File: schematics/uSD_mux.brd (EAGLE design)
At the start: 43.5 x 43.2 mm, 15 parts

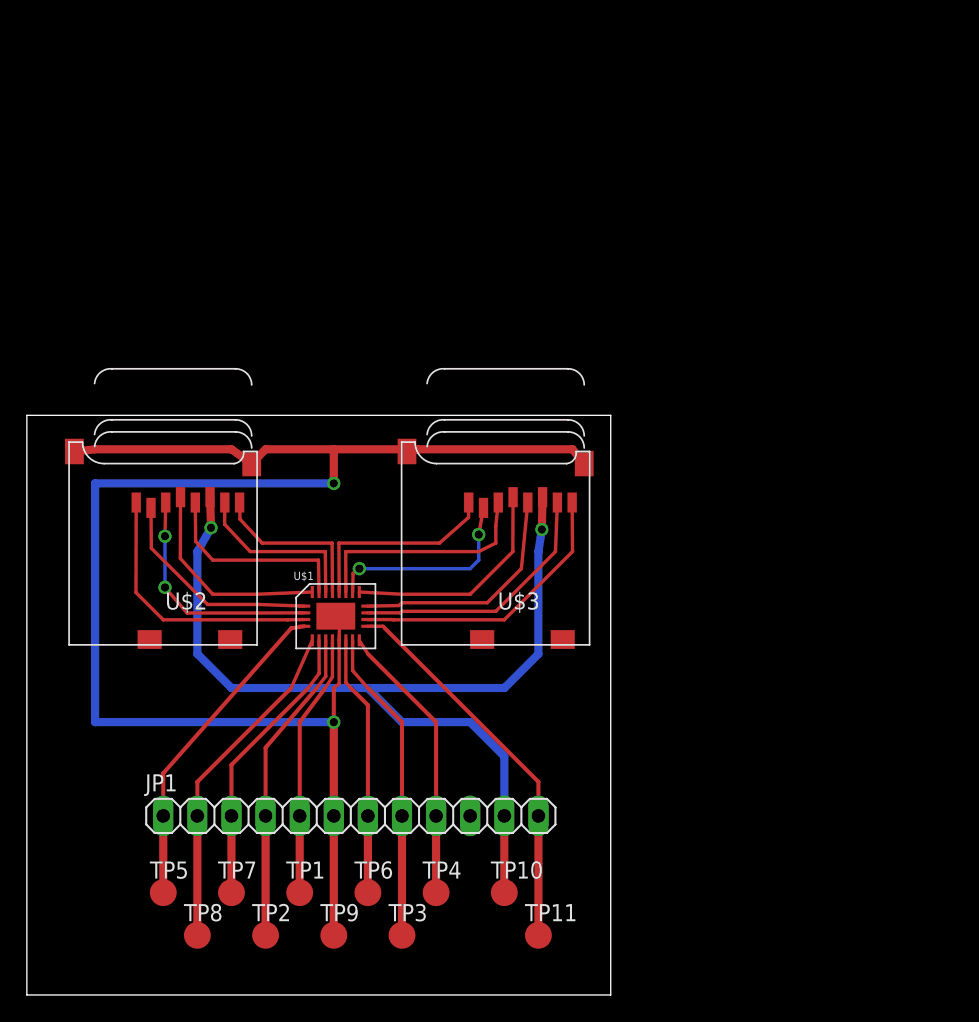
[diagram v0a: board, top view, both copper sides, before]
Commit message: Updated uSD mux board
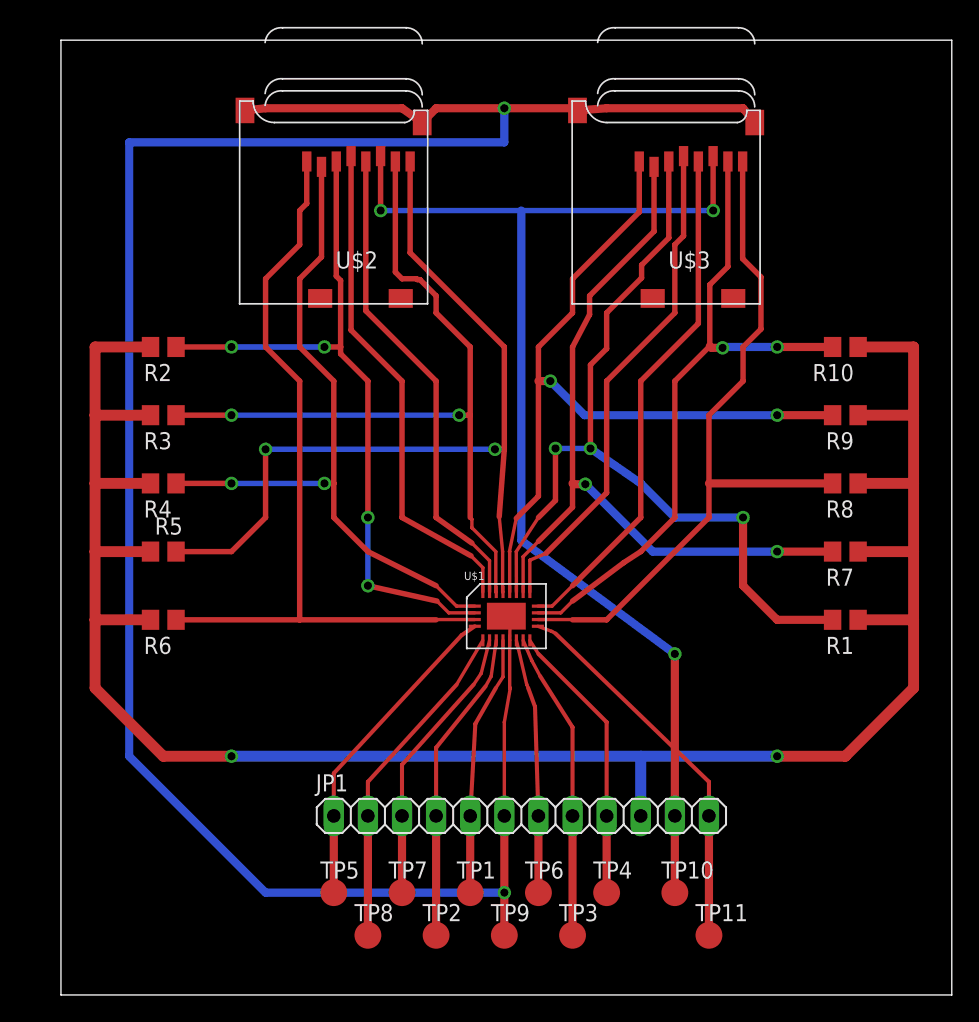
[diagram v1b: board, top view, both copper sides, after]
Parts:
- added R1, R10, R2, R3, R4, R5, R6, R7, R8, R9: 97k, rcl:R0805
- moved U$2 28.4 mm to (29.8, 51.4)
- moved U$3 28.4 mm to (54.6, 51.4)
- moved TP1 12.7 mm to (33.0, 7.62)
- moved TP6 12.7 mm to (38.1, 7.62)
- moved TP9 12.7 mm to (35.6, 4.45)
- moved U$1 12.7 mm to (35.6, 29.2)
- moved TP7 12.7 mm to (27.9, 7.62)
- moved JP1 12.7 mm to (36.8, 13.3)
- moved TP2 12.7 mm to (30.5, 4.45)
- moved TP3 12.7 mm to (40.6, 4.45)
- moved TP4 12.7 mm to (43.2, 7.62)
- moved TP5 12.7 mm to (22.9, 7.62)
- moved TP8 12.7 mm to (25.4, 4.45)
- moved TP10 12.7 mm to (48.3, 7.62)
- moved TP11 12.7 mm to (50.8, 4.45)
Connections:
- new net N$1: JP1.10, R1.1, R10.1, R2.2, R3.2, R4.2, R5.1, R6.2, R7.1, R8.1, R9.1
- net N$10: now also R8.2
- net N$11: now also R9.2
- net N$12: now also R1.2
- net N$2: now also R4.1
- net N$3: now also R3.1
- net N$4: now also R5.2
- net N$5: now also R6.1
- net N$6: now also R2.1
- net N$8: now also R7.2
- net N$9: now also R10.2
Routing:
- net N$1: track 0.00 -> 161.7 mm, vias 0 -> 2
- net N$4: track 12.5 -> 65.6 mm, vias 0 -> 2
- net GND: track 119.2 -> 171.5 mm
- net N$12: track 17.4 -> 64.1 mm, vias 0 -> 3
- net N$3: track 13.0 -> 57.9 mm, vias 0 -> 2
- net N$11: track 15.1 -> 58.9 mm, vias 0 -> 2
- net N$8: track 15.0 -> 57.0 mm
- net N$5: track 20.1 -> 58.7 mm
- net N$2: track 16.1 -> 52.4 mm, vias 0 -> 2
- net N$6: track 17.6 -> 53.3 mm, vias 2 -> 4
- net N$10: track 21.0 -> 53.8 mm
- net N$9: track 19.6 -> 50.2 mm, vias 0 -> 2
- net VDDC1: track 15.6 -> 37.4 mm
- net N$13: track 17.5 -> 38.7 mm
- net N$7: track 15.0 -> 36.1 mm
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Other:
- board size 43.5 x 43.2 mm -> 66.3 x 71.1 mm

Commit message: Updated uSD mux board layout
Forgot to check oshpark DRU before committing first time.  Made
revisions necessary to board layout to meet oshparks design rules.
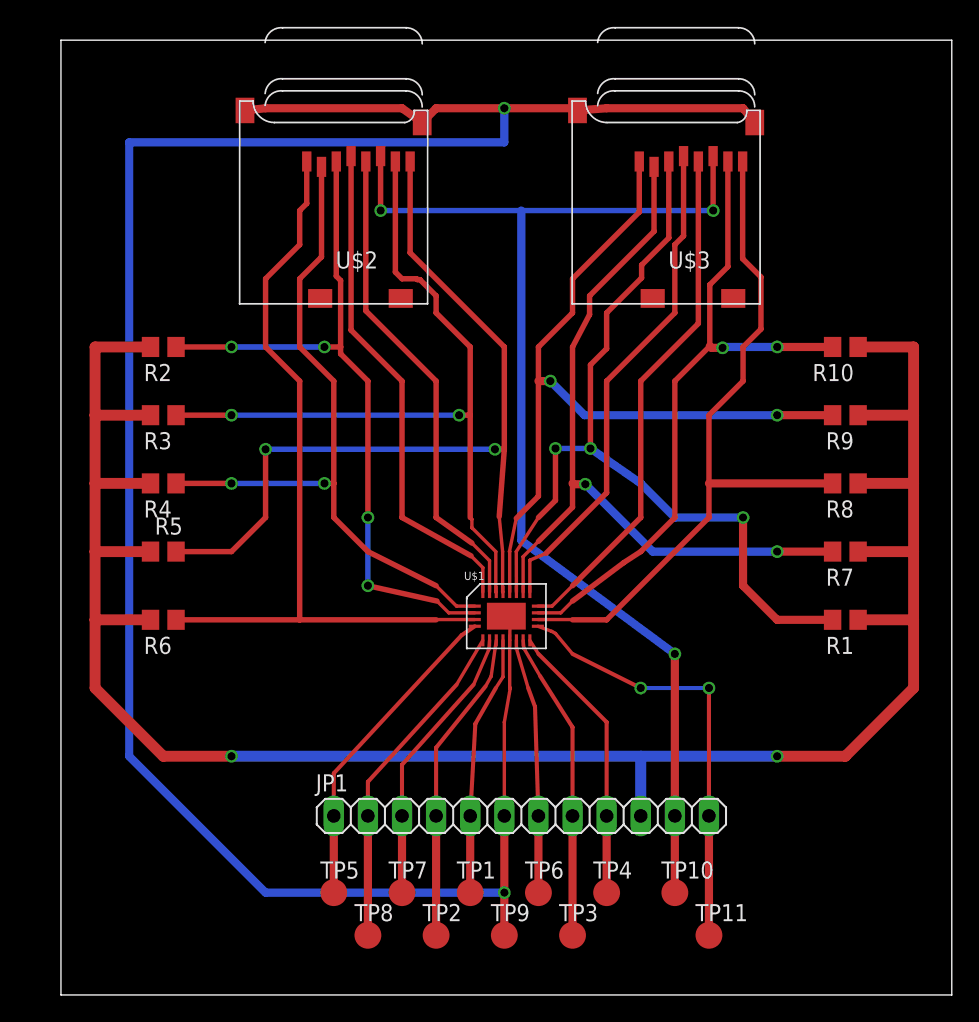
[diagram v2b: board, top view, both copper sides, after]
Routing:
- net S: track 28.7 -> 32.6 mm, vias 0 -> 2
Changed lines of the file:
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@@
 </class>
 </classes>
-<designrules name="epl-lpkf *">
-<description language="en">&lt;b&gt;EAGLE Design Rules for PSU Electronics Prototyping Lab&lt;/b&gt;
+<designrules name="LaenPCBOrder">
+<description language="de">&lt;b&gt;EAGLE Design Rules&lt;/b&gt;
 &lt;p&gt;
-2013-03-03: Modified from  &lt;b&gt;sunstone_quickturn.dru&lt;/b&gt; to meet minimum drills and spacing for the LPKF S63 Circuit Board Router.
-&lt;/p&gt;</description>
+Die Standard-Design-Rules sind so gewählt, dass sie für
+die meisten Anwendungen passen. Sollte ihre Platine
+besondere Anforderungen haben, treffen Sie die erforderlichen
+Einstellungen hier und speichern die Design Rules unter
+einem neuen Namen ab.</description>
+<description language="en">&lt;b&gt;Laen's PCB Order Design Rules&lt;/b&gt;
+&lt;p&gt;
+Please make sure your boards conform to these design rules.</description>
 <param name="layerSetup" value="(1*16)"/>
-<param name="mtCopper" value="0.0178mm 0.0356mm 0.0356mm 0.0356mm 0.0356mm 0.0356mm 0.0356mm 0.0356mm 0.0356mm 0.0356mm 0.0356mm 0.0356mm 0.0356mm 0.0356mm 0.0356mm 0.0178mm"/>
-<param name="mtIsolate" value="59mil 0.1499mm 0.2007mm 0.1499mm 0.2007mm 0.1499mm 0.2007mm 0.1499mm 0.2007mm 0.1499mm 0.2007mm 0.1499mm 0.2007mm 0.1499mm 0.2007mm"/>
-<param name="mdWireWire" value="0.34798125mm"/>
+<param name="mtCopper" value="0.0356mm 0.0356mm 0.0356mm 0.0356mm 0.0356mm 0.0356mm 0.0356mm 0.0356mm 0.0356mm 0.0356mm 0.0356mm 0.0356mm 0.0356mm 0.0356mm 0.0356mm 0.0356mm"/>
+<param name="mtIsolate" value="1.5011mm 0.1499mm 0.2007mm 0.1499mm 0.2007mm 0.1499mm 0.2007mm 0.1499mm 0.2007mm 0.1499mm 0.2007mm 0.1499mm 0.2007mm 0.1499mm 0.2007mm"/>
+<param name="mdWireWire" value="6mil"/>
 <param name="mdWirePad" value="6mil"/>
 <param name="mdWireVia" value="6mil"/>
@@
 <param name="mnLayersViaInSmd" value="2"/>
 <param name="mdCopperDimension" value="15mil"/>
-<param name="mdDrill" value="15mil"/>
+<param name="mdDrill" value="6mil"/>
 <param name="mdSmdStop" value="0mil"/>
-<param name="msWidth" value="8mil"/>
-<param name="msDrill" value="0.35mm"/>
-<param name="msMicroVia" value="9.9898mm"/>
+<param name="msWidth" value="6mil"/>
+<param name="msDrill" value="13mil"/>
+<param name="msMicroVia" value="13mil"/>
 <param name="msBlindViaRatio" value="0.5"/>
 <param name="rvPadTop" value="0.25"/>
@@
 <param name="rvMicroViaOuter" value="0.25"/>
 <param name="rvMicroViaInner" value="0.25"/>
-<param name="rlMinPadTop" value="8mil"/>
-<param name="rlMaxPadTop" value="999mil"/>
-<param name="rlMinPadInner" value="0mil"/>
-<param name="rlMaxPadInner" value="0mil"/>
-<param name="rlMinPadBottom" value="8mil"/>
-<param name="rlMaxPadBottom" value="999mil"/>
-<param name="rlMinViaOuter" value="8mil"/>
-<param name="rlMaxViaOuter" value="999mil"/>
-<param name="rlMinViaInner" value="0mil"/>
-<param name="rlMaxViaInner" value="0mil"/>
-<param name="rlMinMicroViaOuter" value="8mil"/>
-<param name="rlMaxMicroViaOuter" value="999mil"/>
-<param name="rlMinMicroViaInner" value="0mil"/>
-<param name="rlMaxMicroViaInner" value="0mil"/>
+<param name="rlMinPadTop" value="7mil"/>
+<param name="rlMaxPadTop" value="20mil"/>
+<param name="rlMinPadInner" value="7mil"/>
+<param name="rlMaxPadInner" value="20mil"/>
+<param name="rlMinPadBottom" value="7mil"/>
+<param name="rlMaxPadBottom" value="20mil"/>
+<param name="rlMinViaOuter" value="7mil"/>
+<param name="rlMaxViaOuter" value="20mil"/>
+<param name="rlMinViaInner" value="7mil"/>
+<param name="rlMaxViaInner" value="20mil"/>
+<param name="rlMinMicroViaOuter" value="4mil"/>
+<param name="rlMaxMicroViaOuter" value="20mil"/>
+<param name="rlMinMicroViaInner" value="4mil"/>
+<param name="rlMaxMicroViaInner" value="20mil"/>
 <param name="psTop" value="-1"/>
 <param name="psBottom" value="-1"/>
@@
 <param name="checkRestrict" value="1"/>
 <param name="useDiameter" value="13"/>
-<param name="maxErrors" value="500"/>
+<param name="maxErrors" value="50"/>
 </designrules>
 <autorouter>
@@
 <contactref element="TP7" pad="TP"/>
 <wire x1="27.94" y1="13.335" x2="27.94" y2="7.62" width="0.6096" layer="1"/>
-<wire x1="33.274" y1="23.114" x2="33.835" y2="23.95" width="0.254" layer="1"/>
-<wire x1="33.835" y1="23.95" x2="34.46" y2="26.41" width="0.254" layer="1"/>
+<wire x1="33.274" y1="23.114" x2="34.4065" y2="25.728" width="0.254" layer="1"/>
+<wire x1="34.4065" y1="25.728" x2="34.46" y2="26.41" width="0.254" layer="1"/>
 </signal>
 <signal name="CMD">
@@
 <contactref element="TP6" pad="TP"/>
 <wire x1="38.1" y1="13.335" x2="38.1" y2="7.62" width="0.6096" layer="1"/>
-<wire x1="37.338" y1="22.86" x2="37.222" y2="23.143" width="0.254" layer="1"/>
-<wire x1="37.222" y1="23.143" x2="36.46" y2="26.41" width="0.254" layer="1"/>
+<wire x1="37.338" y1="22.86" x2="36.46" y2="25.81" width="0.254" layer="1"/>
+<wire x1="36.46" y1="25.81" x2="36.46" y2="26.41" width="0.254" layer="1"/>
 </signal>
 <signal name="DAT0">
@@
 <contactref element="TP3" pad="TP"/>
 <wire x1="40.64" y1="13.335" x2="40.64" y2="4.445" width="0.6096" layer="1"/>
-<wire x1="38.227" y1="23.749" x2="37.595" y2="24.922" width="0.254" layer="1"/>
-<wire x1="37.595" y1="24.922" x2="36.96" y2="26.41" width="0.254" layer="1"/>
+<wire x1="38.227" y1="23.749" x2="37.0235" y2="25.811" width="0.254" layer="1"/>
+<wire x1="37.0235" y1="25.811" x2="36.96" y2="26.41" width="0.254" layer="1"/>
 </signal>
 <signal name="DAT1">
@@
 <contactref element="U$1" pad="S"/>
 <contactref element="JP1" pad="12"/>
-<wire x1="39.37" y1="26.924" x2="50.8" y2="15.875" width="0.3048" layer="1"/>
-<wire x1="50.8" y1="15.875" x2="50.8" y2="13.335" width="0.3048" layer="1"/>
 <contactref element="TP11" pad="TP"/>
 <wire x1="50.8" y1="13.335" x2="50.8" y2="4.445" width="0.6096" layer="1"/>
 <wire x1="39.37" y1="26.924" x2="39.093" y2="27.079" width="0.254" layer="1"/>
 <wire x1="39.093" y1="27.079" x2="38.06" y2="27.46" width="0.254" layer="1"/>
+<wire x1="39.37" y1="26.924" x2="40.64" y2="25.4" width="0.254" layer="1"/>
+<wire x1="40.64" y1="25.4" x2="45.72" y2="22.86" width="0.3048" layer="1"/>
+<via x="45.72" y="22.86" extent="1-16" drill="0.6" shape="square"/>
+<wire x1="45.72" y1="22.86" x2="50.8" y2="22.86" width="0.3048" layer="16"/>
+<via x="50.8" y="22.86" extent="1-16" drill="0.6" shape="square"/>
+<wire x1="50.8" y1="22.86" x2="50.8" y2="13.335" width="0.3048" layer="1"/>
 </signal>
 <signal name="VSS">

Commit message: Updated uSD mux sch/brd files
Added decoupling capacitors, labeled +3.6V connection on 12 pin
connector.
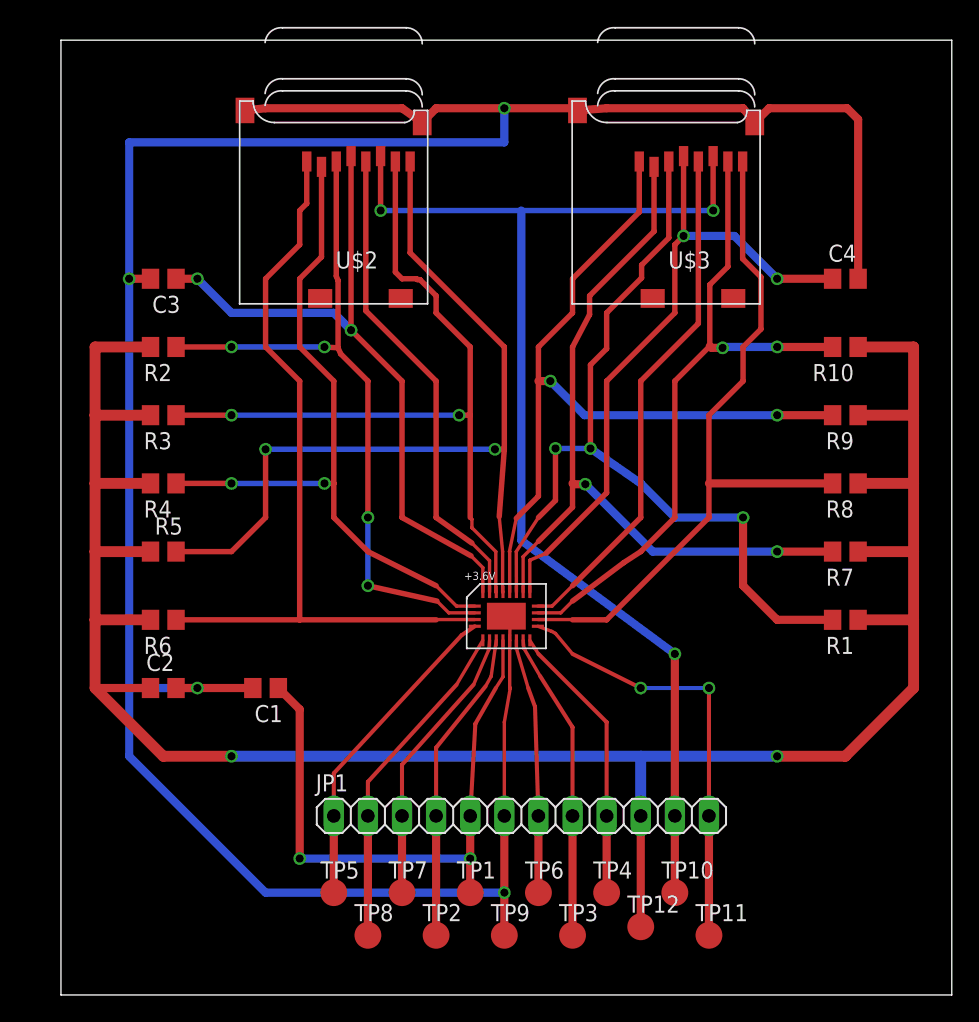
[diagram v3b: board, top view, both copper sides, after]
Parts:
- added C1, C2, C3, C4: (no value), rcl:C0805
- added TP12: TPTP20R, testpad:TP20R
- renumbered U$1 to +3.6V
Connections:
- net GND: now also C1.2, C2.2, C3.2, C4.2
- net N$1: now also C2.1, TP12.TP
- net VDDC1: now also C3.1
- net VDDC2: now also C4.1
- net VDDH: now also C1.1
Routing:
- net GND: track 171.5 -> 204.3 mm, vias 2 -> 4
- net VDDH: track 19.4 -> 45.4 mm, vias 0 -> 2
- net VDDC1: track 37.4 -> 52.0 mm, vias 0 -> 2
- net VDDC2: track 37.5 -> 49.9 mm, vias 0 -> 2
- net N$1: track 161.7 -> 174.1 mm

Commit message: Updated uSD board layout
Board was excessively expensive, changed board layout to reduce surface
area --> cheaper fab . Previous iteration was quoted $37 at oshpark,
updated board $25.
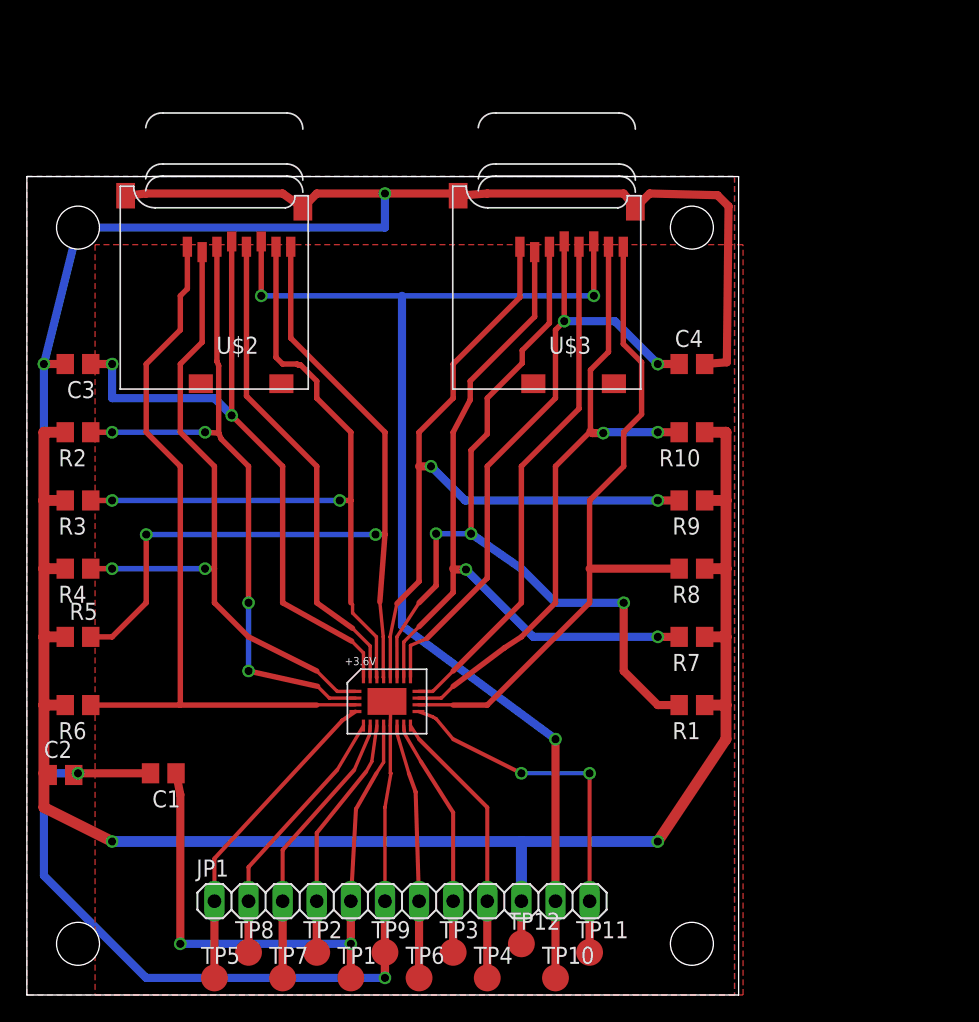
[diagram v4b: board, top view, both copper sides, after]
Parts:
- moved C4 13.1 mm to (49.5, 47.0)
- moved R1 13.1 mm to (49.5, 21.6)
- moved R10 13.1 mm to (49.5, 41.9)
- moved R7 13.1 mm to (49.5, 26.7)
- moved R8 13.1 mm to (49.5, 31.8)
- moved R9 13.1 mm to (49.5, 36.8)
- moved TP1 10.9 mm to (24.1, 1.27)
- moved +3.6V 10.9 mm to (26.7, 22.9)
- moved U$2 10.9 mm to (21.0, 45.1)
- moved U$3 10.9 mm to (45.7, 45.1)
- moved TP10 10.9 mm to (39.4, 1.27)
- moved TP4 10.9 mm to (34.3, 1.27)
- moved TP6 10.9 mm to (29.2, 1.27)
- moved TP7 10.9 mm to (19.1, 1.27)
- moved JP1 10.9 mm to (27.9, 6.99)
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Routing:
- net N$1: track 174.1 -> 130.1 mm
- net GND: track 204.3 -> 195.3 mm
- net S: track 32.6 -> 27.5 mm
- net DAT2: track 25.1 -> 20.0 mm
- net DAT0: track 23.0 -> 17.9 mm
- net CMD: track 23.4 -> 18.3 mm
- net N$3: track 57.9 -> 55.3 mm
- net VDDC2: track 49.9 -> 47.4 mm
- net N$9: track 50.2 -> 47.6 mm
- net N$2: track 52.4 -> 49.8 mm
- net N$8: track 57.0 -> 54.4 mm
- net N$4: track 65.6 -> 63.1 mm
- net N$10: track 53.8 -> 51.3 mm
- net N$6: track 53.0 -> 50.5 mm
- net N$5: track 58.7 -> 56.2 mm
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- added copper zone on layer 1, net GND
- added copper zone on layer 16, net GND
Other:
- board size 66.3 x 71.1 mm -> 53 x 61 mm
